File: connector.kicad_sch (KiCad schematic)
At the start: 2 parts, among them J1 Conn_02x20_Odd_Even, J2 Conn_01x02

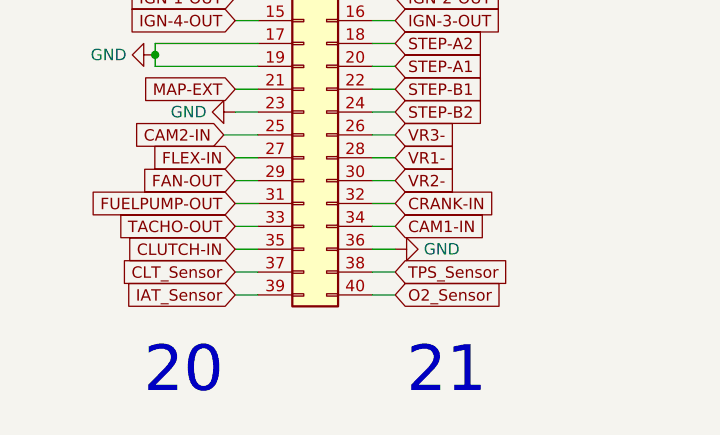
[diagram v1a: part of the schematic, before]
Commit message: Swapped which angle sensors are connected to VR conditioners
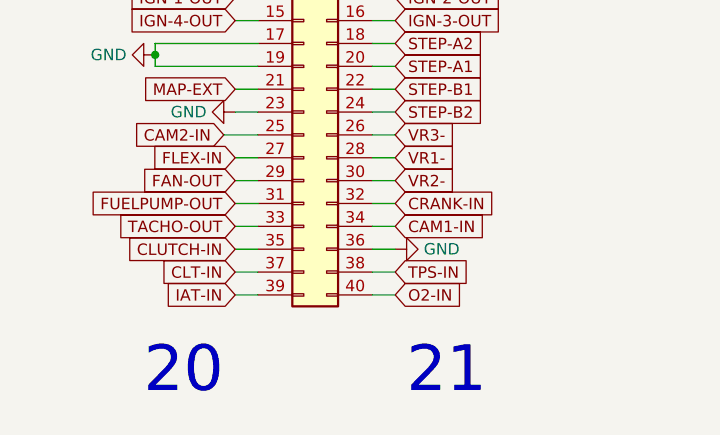
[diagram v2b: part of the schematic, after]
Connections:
- net CLT_Sensor renamed CLT-IN
- net IAT_Sensor renamed IAT-IN
- net O2_Sensor renamed O2-IN
- net TPS_Sensor renamed TPS-IN
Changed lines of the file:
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@@
     (effects (font (size 1.27 1.27)) (justify left bottom))
   )
-  (global_label "O2_Sensor" (shape input) (at 165.1 121.92 0) (fields_autoplaced)
-    (effects (font (size 1.27 1.27)) (justify left))
-    (property "Intersheet References" "${INTERSHEET_REFS}" (id 0) (at 0 0 0)
-      (effects (font (size 1.27 1.27)) hide)
+  (global_label "O2-IN" (shape input) (at 165.1 121.92 0) (fields_autoplaced)
+    (effects (font (size 1.27 1.27)) (justify left))
+    (property "Intersheet References" "${INTERSHEET_REFS}" (id 0) (at 173.5607 121.8406 0)
+      (effects (font (size 1.27 1.27)) (justify left) hide)
     )
   )
@@
     )
   )
-  (global_label "IAT_Sensor" (shape input) (at 147.32 121.92 180) (fields_autoplaced)
-    (effects (font (size 1.27 1.27)) (justify right))
-    (property "Intersheet References" "${INTERSHEET_REFS}" (id 0) (at 0 0 0)
-      (effects (font (size 1.27 1.27)) hide)
+  (global_label "IAT-IN" (shape input) (at 147.32 121.92 180) (fields_autoplaced)
+    (effects (font (size 1.27 1.27)) (justify right))
+    (property "Intersheet References" "${INTERSHEET_REFS}" (id 0) (at 138.7383 121.8406 0)
+      (effects (font (size 1.27 1.27)) (justify right) hide)
     )
   )
@@
     )
   )
-  (global_label "TPS_Sensor" (shape input) (at 165.1 119.38 0) (fields_autoplaced)
-    (effects (font (size 1.27 1.27)) (justify left))
-    (property "Intersheet References" "${INTERSHEET_REFS}" (id 0) (at 0 0 0)
-      (effects (font (size 1.27 1.27)) hide)
+  (global_label "TPS-IN" (shape input) (at 165.1 119.38 0) (fields_autoplaced)
+    (effects (font (size 1.27 1.27)) (justify left))
+    (property "Intersheet References" "${INTERSHEET_REFS}" (id 0) (at 174.4679 119.3006 0)
+      (effects (font (size 1.27 1.27)) (justify left) hide)
     )
   )
@@
     )
   )
-  (global_label "CLT_Sensor" (shape input) (at 147.32 119.38 180) (fields_autoplaced)
-    (effects (font (size 1.27 1.27)) (justify right))
-    (property "Intersheet References" "${INTERSHEET_REFS}" (id 0) (at 0 0 0)
-      (effects (font (size 1.27 1.27)) hide)
-    )
-  )
+  (global_label "CLT-IN" (shape input) (at 147.32 119.38 180) (fields_autoplaced)
+    (effects (font (size 1.27 1.27)) (justify right))
+    (property "Intersheet References" "${INTERSHEET_REFS}" (id 0) (at 138.1336 119.3006 0)
+      (effects (font (size 1.27 1.27)) (justify right) hide)
+    )
+  )
